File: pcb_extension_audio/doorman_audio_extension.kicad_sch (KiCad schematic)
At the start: 42 parts, among them J1 Audio Out, J2 GPIO, J4 Extension Board Connector, J5 Audio In, U1 ES8388

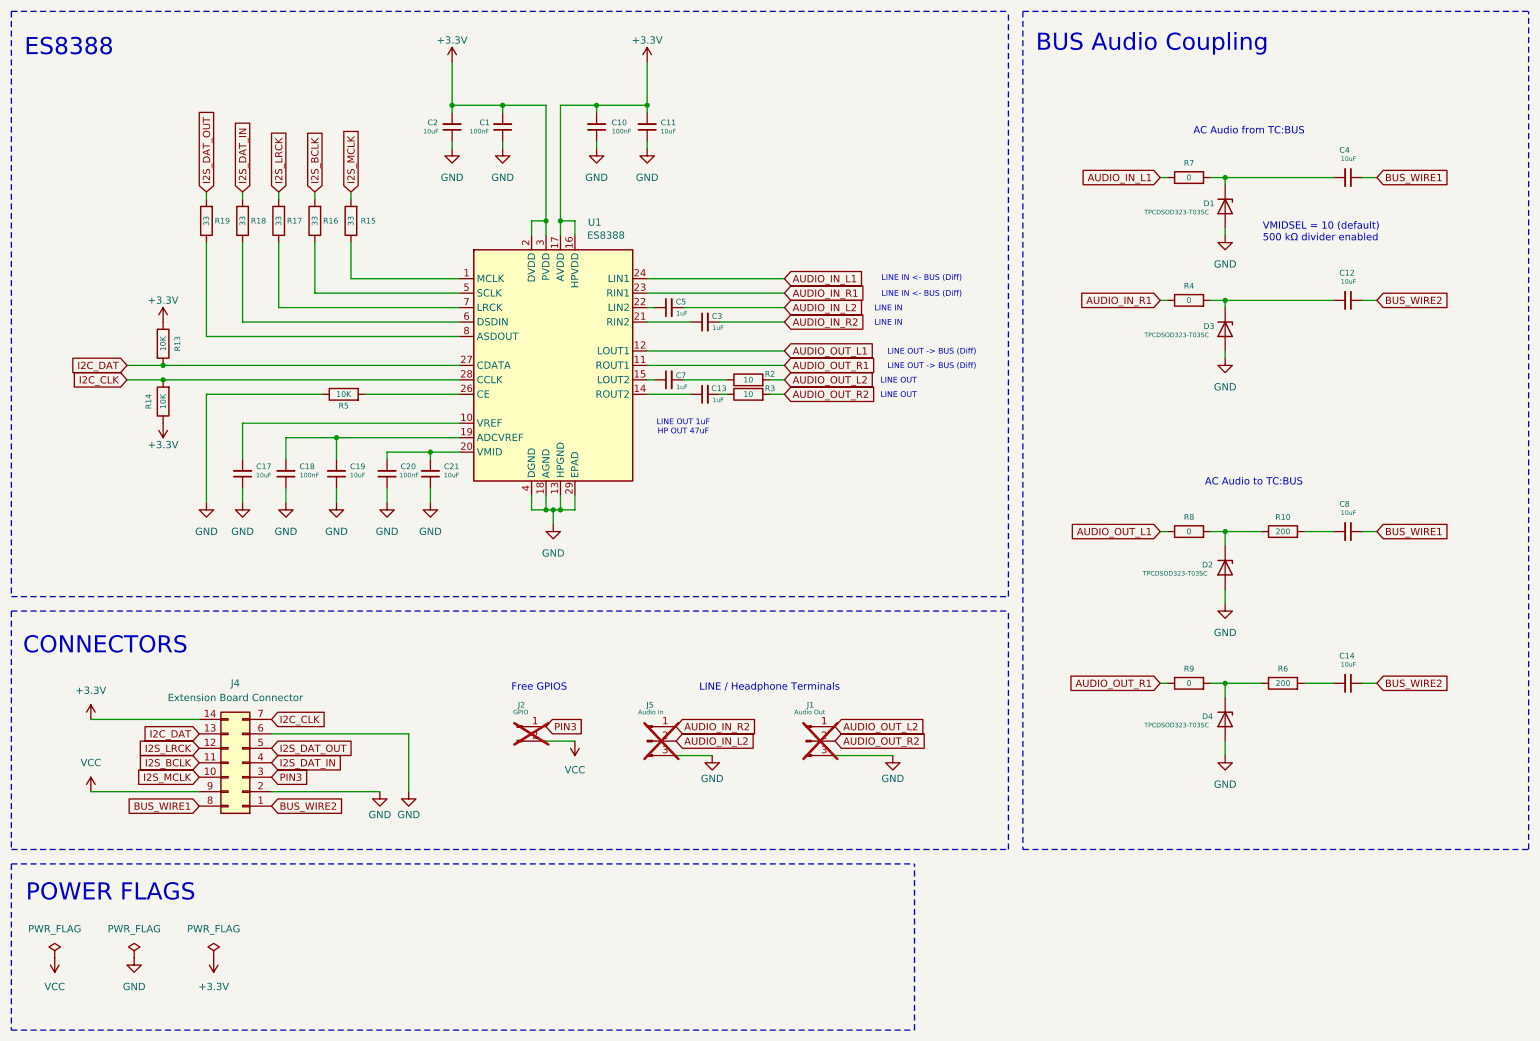
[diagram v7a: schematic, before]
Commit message: WIP virtual devices
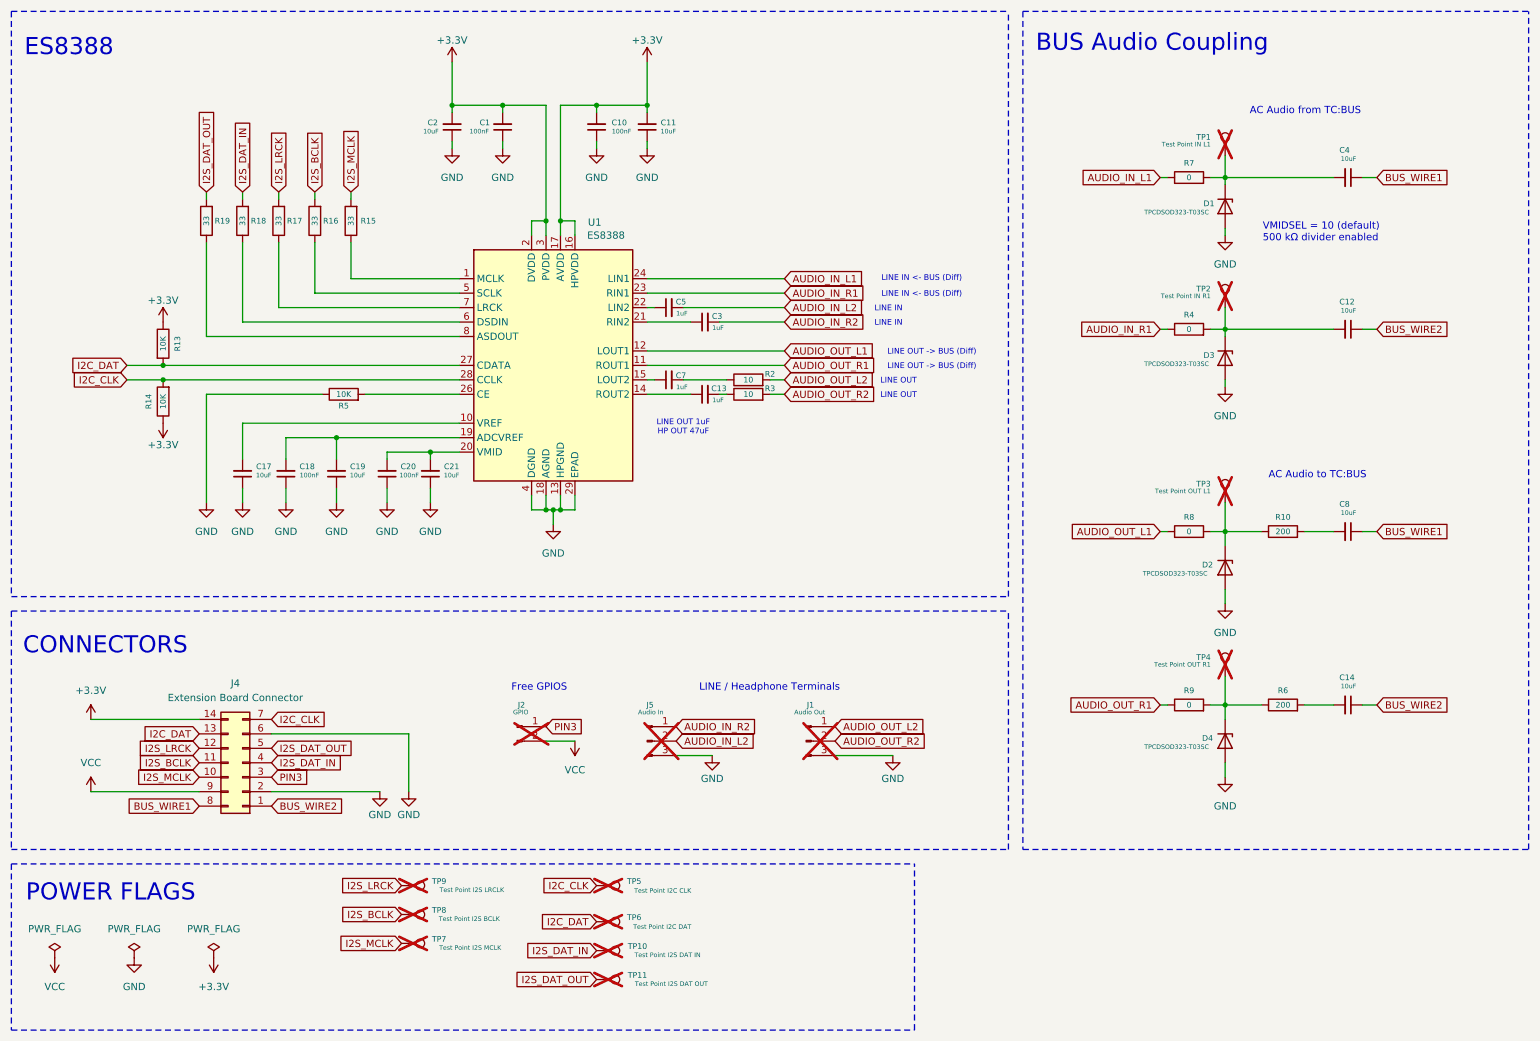
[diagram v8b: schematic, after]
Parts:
- added TP1: Test Point IN L1, TestPoint:TestPoint_Pad_D1.0mm, symbol Connector:TestPoint
- added TP10: Test Point I2S DAT IN, TestPoint:TestPoint_Pad_D1.0mm, symbol Connector:TestPoint
- added TP11: Test Point I2S DAT OUT, TestPoint:TestPoint_Pad_D1.0mm, symbol Connector:TestPoint
- added TP2: Test Point IN R1, TestPoint:TestPoint_Pad_D1.0mm, symbol Connector:TestPoint
- added TP3: Test Point OUT L1, TestPoint:TestPoint_Pad_D1.0mm, symbol Connector:TestPoint
- added TP4: Test Point OUT R1, TestPoint:TestPoint_Pad_D1.0mm, symbol Connector:TestPoint
- added TP5: Test Point I2C CLK, TestPoint:TestPoint_Pad_D1.0mm, symbol Connector:TestPoint
- added TP6: Test Point I2C DAT, TestPoint:TestPoint_Pad_D1.0mm, symbol Connector:TestPoint
- added TP7: Test Point I2S MCLK, TestPoint:TestPoint_Pad_D1.0mm, symbol Connector:TestPoint
- added TP8: Test Point I2S BCLK, TestPoint:TestPoint_Pad_D1.0mm, symbol Connector:TestPoint
- added TP9: Test Point I2S LRCLK, TestPoint:TestPoint_Pad_D1.0mm, symbol Connector:TestPoint
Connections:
- net I2C_CLK: now also TP5.1
- net I2C_DAT: now also TP6.1
- net I2S_BCLK: now also TP8.1
- net I2S_DAT_IN: now also TP10.1
- net I2S_DAT_OUT: now also TP11.1
- net I2S_LRCK: now also TP9.1
- net I2S_MCLK: now also TP7.1
- net at D2.1 (K), R10.1, R8.2: now also TP3.1
- net at C4.2, D1.1 (K), R7.2: now also TP1.1
- net at D4.1 (K), R6.1, R9.2: now also TP4.1
- net at C12.2, D3.1 (K), R4.2: now also TP2.1
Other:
- moved on the sheet: C12, C14, D3, D4, R4, R6, R9
